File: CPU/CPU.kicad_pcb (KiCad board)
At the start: 4 copper layers, 364 x 203 mm, 335 parts, among them J1 Conn_02x36_Top_Bottom, P2 Conn_02x13_Top_Bottom, P3 Conn_02x13_Top_Bottom, P4 IDC-16, P5 Conn_02x25_Counter_Clockwise, P6 Conn_02x25_Counter_Clockwise, P7 Conn_02x07_Counter_Clockwise, P8 Conn_02x08_Odd_Even

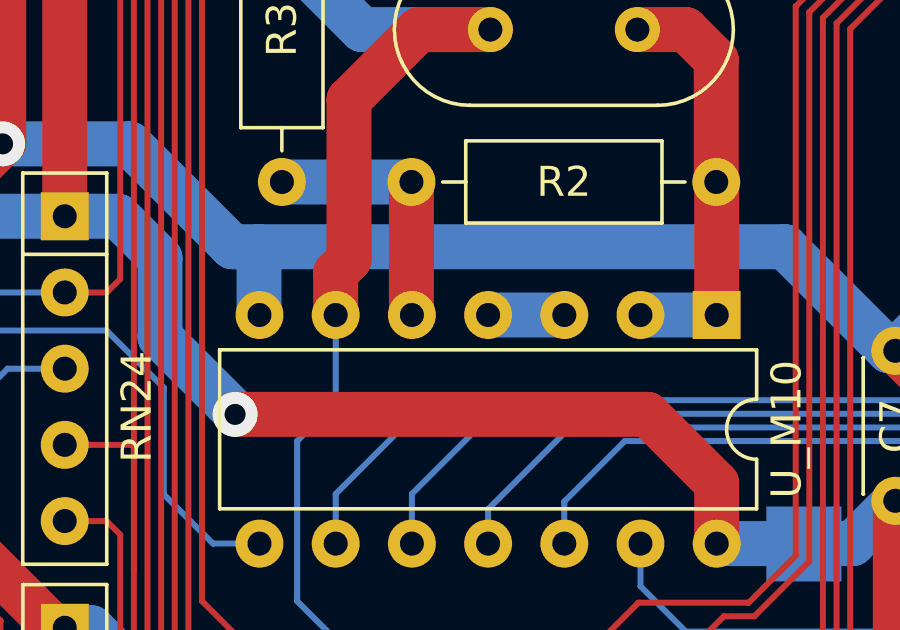
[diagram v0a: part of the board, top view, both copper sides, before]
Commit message: CPU: Add missing connection
CPU-E002: Add missing connection between U_M10 pins 4 and 5.
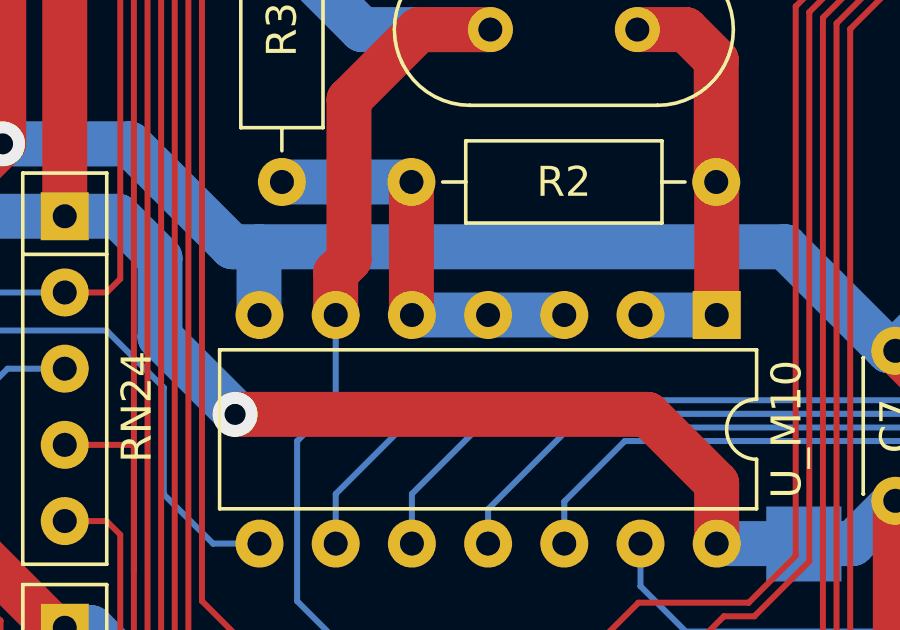
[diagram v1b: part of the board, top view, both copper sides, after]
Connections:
- U_M10 pad 3: Net-(U_M10-Pad3) -> Net-(R2-Pad1)
- U_M10 pad 4: Net-(U_M10-Pad3) -> Net-(R2-Pad1)
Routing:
- net Net-(R2-Pad1): track 8.74 -> 13.8 mm
- net Net-(U_M10-Pad3): track 2.54 -> 0.00 mm

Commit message: CPU: Use HC-49U quartz, placed horizontally
The same as in original schematic. Some layout around has been optimized
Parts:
- C9: footprint Capacitor_THT:C_Rect_L9.0mm_W2.5mm_P7.50mm_MKT -> Capacitor_THT:C_Disc_D4.3mm_W1.9mm_P5.00mm
- R17: footprint Resistor_THT:R_Axial_DIN0204_L3.6mm_D1.6mm_P5.08mm_Horizontal -> Resistor_THT:R_Axial_DIN0204_L3.6mm_D1.6mm_P7.62mm_Horizontal
- XTAL1: footprint Crystal:Crystal_HC18-U_Vertical -> Crystal:Crystal_HC49-U_Horizontal
- moved R17 2.64 mm to (64.4, 188.1)
- moved XTAL1 2.60 mm to (49.4, 154.7), turned to 90 degrees
- moved C9 1.38 mm to (68.4, 194.4)
- moved +5V 0.50 mm to (66.8, 143.4)
- moved C6 0.48 mm to (60.8, 142.1)
- moved C10 0.48 mm to (69.1, 207.8)
- moved R2 0.30 mm to (46.7, 157.2), turned to 90 degrees
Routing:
- net DataP.D_{6}: track 690.6 -> 679.6 mm
- net Net-(R2-Pad2): track 14.1 -> 23.1 mm
- net GND: track 5032.1 -> 5036.8 mm
- net +5V: track 4593.4 -> 4589.3 mm, vias 50 -> 47
- net DataP.D_{7}: track 704.2 -> 706.8 mm
- net Net-(U_M13-Pad5): track 78.4 -> 80.9 mm
- net /RTC_INT: track 230.2 -> 227.9 mm, vias 3 -> 2
- net /~{Reset_{1}}: track 384.9 -> 387.2 mm
- net P7_5: track 45.5 -> 47.5 mm
- net /~{RTC_INT_Reset}: track 69.4 -> 67.6 mm
- net /SW_2: track 138.2 -> 136.4 mm
- net P7_8: track 23.2 -> 21.8 mm, vias 2 -> 1
- net Net-(U_J11-Pad5): track 89.2 -> 90.3 mm
- net Net-(R3-Pad1): track 78.1 -> 77.0 mm
- net /PROM_Disable: track 308.2 -> 307.3 mm
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
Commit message: CPU: Some power layout optimizations
Remove some vias, thicker traces in some places. Some other traces rearranged
to accomodate changes
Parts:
- R18: footprint Resistor_THT:R_Axial_DIN0207_L6.3mm_D2.5mm_P7.62mm_Horizontal -> Resistor_THT:R_Axial_DIN0207_L6.3mm_D2.5mm_P10.16mm_Horizontal
- moved R18 5.43 mm to (309.8, 100.5)
- moved C6 1.09 mm to (61.6, 142.8)
- moved GND 0.84 mm to (279.7, 95.9)
- moved C28 0.61 mm to (274.0, 75.4)
- moved C16 0.09 mm to (136.7, 128.6)
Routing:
- net +5V: track 4589.3 -> 4566.7 mm, vias 47 -> 42
- net Address.A_{8}: track 155.9 -> 165.8 mm
- net /~{Reset_{2}}: track 533.0 -> 541.6 mm
- net GND: track 5036.8 -> 5030.5 mm, vias 69 -> 59
- net Address.A_{4}: track 114.7 -> 120.4 mm, vias 1 -> 2
- net Address.A_{10}: track 145.8 -> 140.5 mm, vias 5 -> 3
- net Net-(U_B2-Pad7): track 166.7 -> 171.7 mm
- net /~{DataEndCycle}: track 325.7 -> 330.6 mm
- net /~{DataReady}: track 316.6 -> 321.4 mm
- net MW.D3_{4}: track 142.5 -> 138.0 mm
- net Net-(U_B6-Pad10): track 84.1 -> 79.7 mm
- net MW.E2_{3}: track 197.4 -> 201.7 mm
- net /~{MainClockPhi1}: track 400.7 -> 404.6 mm
- net /K7_S_{1}: track 61.9 -> 58.0 mm
- net Net-(U_B1-Pad7): track 178.1 -> 174.2 mm, vias 0 -> 1
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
